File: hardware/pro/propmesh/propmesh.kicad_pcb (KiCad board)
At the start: 4 copper layers, 130 x 100 mm, 265 parts, among them CN1 LINE_OUT, J1 TYPE-C-31-M-12, J10 LED_OUT, J11 LED_OUT, J12 LED_OUT, J13 LED_OUT, J14 RELAY_OUT, J15 RELAY_OUT, J16 RELAY_OUT, J17 DC_IN, J18 DC_JACK, J19 SOCKET_1x8, J2 SERVO, J20 SOCKET_1x8, J21 DIAG_AUX, J22 SOCKET_1x8, J23 MOTOR_OUT, J24 SOCKET_1x8, J25 STEPPER_COIL, J26 DIAG_AUX, J27 STEPPER_COIL, J28 MOTOR_OUT, J29 MS_SEL, J3 SERVO, J30 MS_SEL, J31 MS_SEL, J32 MS_SEL, J33 MS_SEL, J34 MS_SEL, J35 SPEAKER, J36 LED2_SIG, J37 LED1_SIG, J38 LED1_PWR, J39 LED2_PWR, J4 SERVO, J40 ANA_IN, J41 DIG_IN, J42 EXPANSION, J43 ANA_IN, J44 DIG_IN, J45 DIG_IN, J46 PIR_HDR, J47 QWIIC, J48 JP_VIN, J49 JP_5V, J5 SERVO, J50 JP_3V3, J51 JP_USB, J6 SERVO, J7 SERVO, J8 LED_OUT, J9 LED_OUT, K1 HK4100F-DC5V-SHG, K2 HK4100F-DC5V-SHG, K3 HK4100F-DC5V-SHG, Q1 SI2356DS, Q2 SI2356DS, Q3 SI2356DS, Q4 SI2356DS, Q5 SI2356DS, Q6 SI2356DS, Q7 AOD4185, Q8 AO3400A, SW1 TS-1187A, SW2 TS-1187A, U1 USBLC6-2SC6, U10 PCM5102APWR, U11 SN74AHCT541, U12 PCA9685PW, U2 ESP32-S3-WROOM-1U-N8R2, U3 ULN2003A, U4 PCA9685PW, U5 AP64350SP-13, U6 TLV62569DBV, U7 DRV8871DDAR, U8 DRV8871DDAR, U9 MAX98357AETE+T

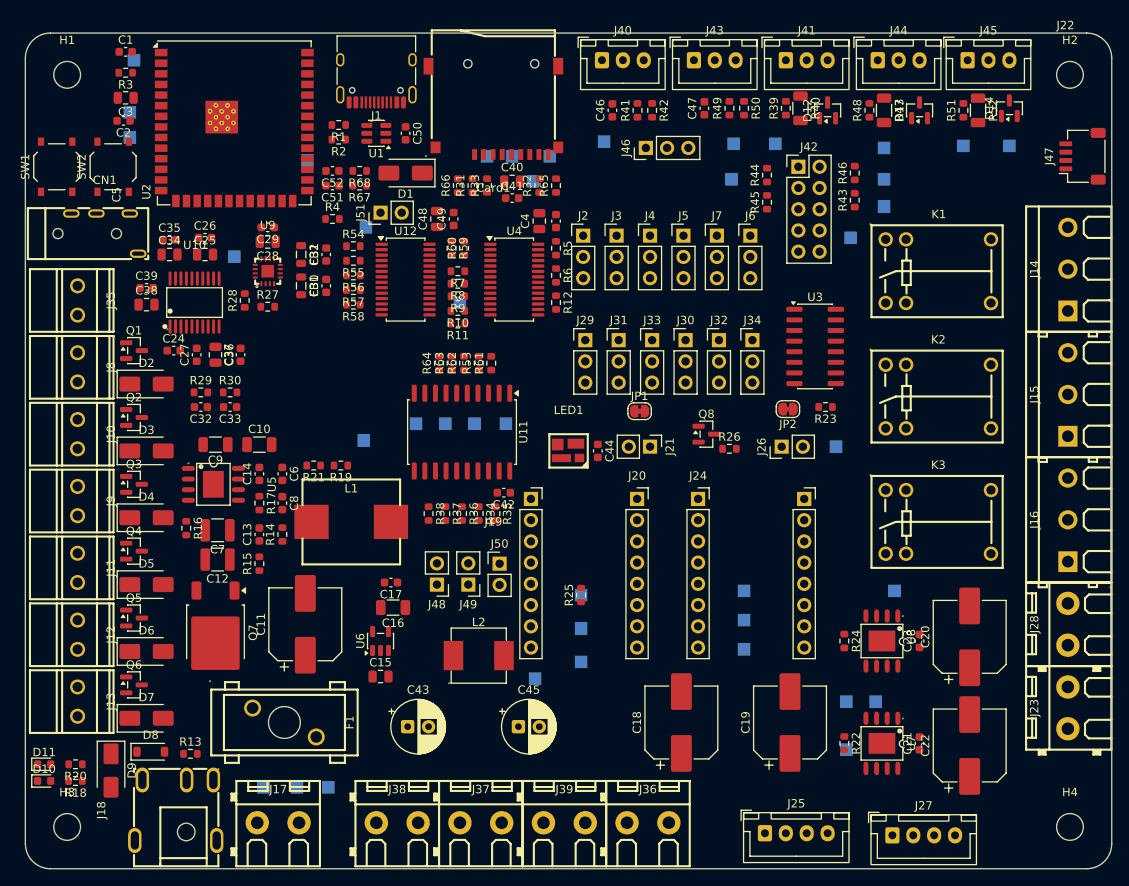
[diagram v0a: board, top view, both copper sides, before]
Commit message: Pro v0.1 pours: 10 zones with 0/45/90 outlines; neck-down and pre-defined sizes check
- tools/makezones.py builds every zone from the board as placed: In1 GND,
  In2 split VIN_PROT / +5V / +3V3 traced on a 2 mm grid with straight and
  45-degree edges only (38-63 corners per region, was 200-380 curved),
  pads the coarse grid lost flipped back, F.Cu GND + 10 A input pours,
  B.Cu GND under the DRV8871s, U.FL keep-out; writes zones-In2-split.png
  from the installed zones. Hand-renamed zones are left alone.
- Colin's hand-simplified In2 regions; layout.md A22 lists what each
  region must enclose and the fix-ups, by net name.
- layout.md: wide track into a small pad (neck-down) recipe; A21
  pre-defined track/via sizes now checked by checksetup.py.
- Mini: solar-charging options note (panel sizing for October sun,
  DFR0559 / CN3791 / on-board TP4056).

DRC: 3 accepted courtyard overlaps, parity 0.

Co-Authored-By: Claude Opus 5.5 <noreply@anthropic.com>
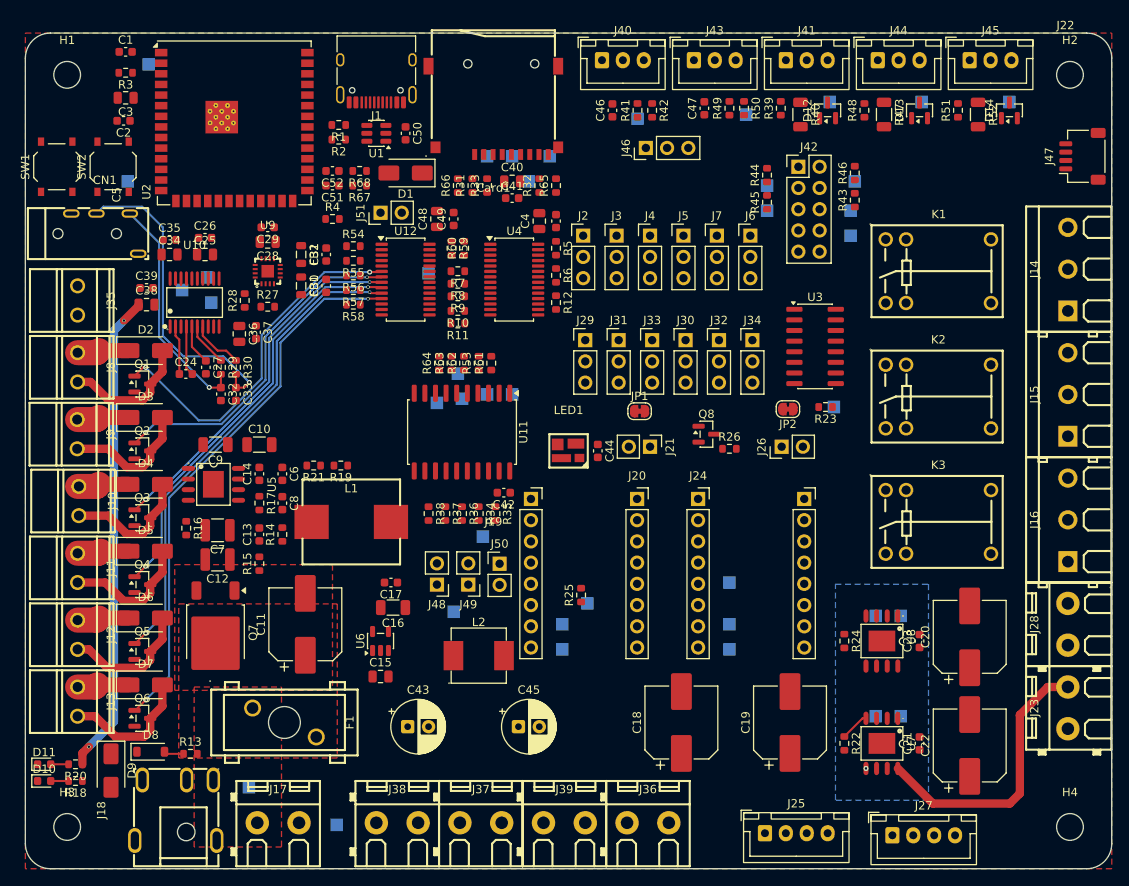
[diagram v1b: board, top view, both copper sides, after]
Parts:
- moved TP38 37.0 mm to (121.0, 115.5)
- moved TP12 30.0 mm to (158.5, 67.5)
- moved TP3 29.0 mm to (82.0, 64.0)
- moved TP18 22.2 mm to (88.5, 77.0)
- moved TP19 22.0 mm to (92.0, 78.5)
- moved TP1 19.8 mm to (118.0, 75.0)
- moved TP37 16.7 mm to (103.0, 120.5)
- moved TP23 16.4 mm to (171.5, 116.0)
- moved TP6 15.7 mm to (125.0, 89.5)
- moved TP39 13.7 mm to (124.5, 106.5)
- moved TP13 8.20 mm to (166.0, 54.5)
- moved J10 8.00 mm to (76.2, 102.2)
- moved J9 8.00 mm to (76.0, 94.2)
- moved TP15 7.60 mm to (187.5, 54.5)
- moved TP14 7.11 mm to (177.0, 54.5)
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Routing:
- net /Outputs/LED_6: track 0.00 -> 65.6 mm, vias 0 -> 2
- net /Outputs/LED_5: track 0.00 -> 58.3 mm, vias 0 -> 2
- net +3V3: track 0.00 -> 57.8 mm, vias 0 -> 2
- net /Outputs/LED_4: track 0.00 -> 50.9 mm, vias 0 -> 2
- net /Outputs/LED_3: track 0.00 -> 43.9 mm, vias 0 -> 2
- net /Outputs/LED_1: track 0.00 -> 43.1 mm, vias 0 -> 2
- net /Outputs/LED_2: track 0.00 -> 40.9 mm, vias 0 -> 2
- net /Audio/LINE_R: track 0.00 -> 38.4 mm, vias 0 -> 1
- net VIN_PROT: track 0.00 -> 37.5 mm, vias 0 -> 1
- net /Motors/MA_OUT2: track 0.00 -> 33.4 mm
- net /Audio/LINE_L: track 0.00 -> 27.7 mm, vias 0 -> 1
- net /Outputs/LED6_K: track 0.00 -> 16.1 mm
- net /Outputs/LED5_K: track 0.00 -> 15.6 mm
- net /Outputs/LED4_K: track 0.00 -> 15.6 mm
- net /Outputs/LED3_K: track 0.00 -> 15.6 mm
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- added copper zone on In2.Cu, net +3V3
- added copper zone on In2.Cu, net +5V
- added copper zone on F.Cu, net /Power/VIN_FUSED
- added copper zone on B.Cu, net GND
- added copper zone on F.Cu, net GND
- added copper zone on In1.Cu, net GND
- added copper zone on F.Cu, net VIN_PROT
- added copper zone on In2.Cu, net VIN_PROT
- added copper zone on F.Cu, net VIN_RAW
